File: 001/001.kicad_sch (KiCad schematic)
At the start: 16 parts, among them P1 Digital, P10 CONN_01X01, P11 CONN_01X01, P12 CONN_01X01, P13 CONN_01X01, P2 Power, P3 Analog, P4 Analog, P5 PWM, P6 PWM, P7 Communication, P8 CONN_01X01, P9 CONN_01X01

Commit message: 半分終了
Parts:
- added C?: 0.1uF, symbol akizuki:C
- added D? (x3): 1N4148, Diode_THT:D_DO-35_SOD27_P7.62mm_Horizontal, symbol Diode:1N4148
- added J?: GPS, symbol Connector_Generic:Conn_01x05
- added J?: iM920, symbol Connector_Generic:Conn_01x07
- added R? (x5): 10k, symbol Device:R_US
- added U?: 24LC256, symbol Memory_EEPROM:24LC256
- R?: value R_US -> 10k
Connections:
- net 19(Rx1) is gone; now on net 15(Rx3): P7.6 (Pin_6)
- net +3V3: now also J?.4 (Pin_4), R?.1, R?.1, R?.1
- net +5V: now also C?.2, J?.5 (Pin_5), R?.1, R?.1, U?.8 (VCC)
- net 14(Tx3): now also D?.1 (K)
- net 15(Rx3): now also J?.3 (Pin_3), J?.5 (Pin_5)
- net 18(Tx1): now also D?.1 (K)
- net 2(**): now also J?.2 (Pin_2)
- net 3(**): now also D?.1 (K)
- net 4(**): now also J?.1 (Pin_1)
- net 5(**): now also J?.7 (Pin_7)
- net GND: now also C?.1, J?.3 (Pin_3), J?.4 (Pin_4), U?.1 (A0), U?.2 (A1), U?.3 (A2), U?.4 (GND), U?.7 (WP)
- net SCL: now also R?.2, U?.6 (SCL)
- net SDA: now also R?.2, U?.5 (SDA)
- new net !RESET: D?.2 (A), J?.1 (Pin_1), R?.2
- new net RX: D?.2 (A), D?.2 (A), J?.2 (Pin_2), J?.6 (Pin_6), R?.2, R?.2
- no-connect marks 7 -> 12
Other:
- moved on the sheet: U?

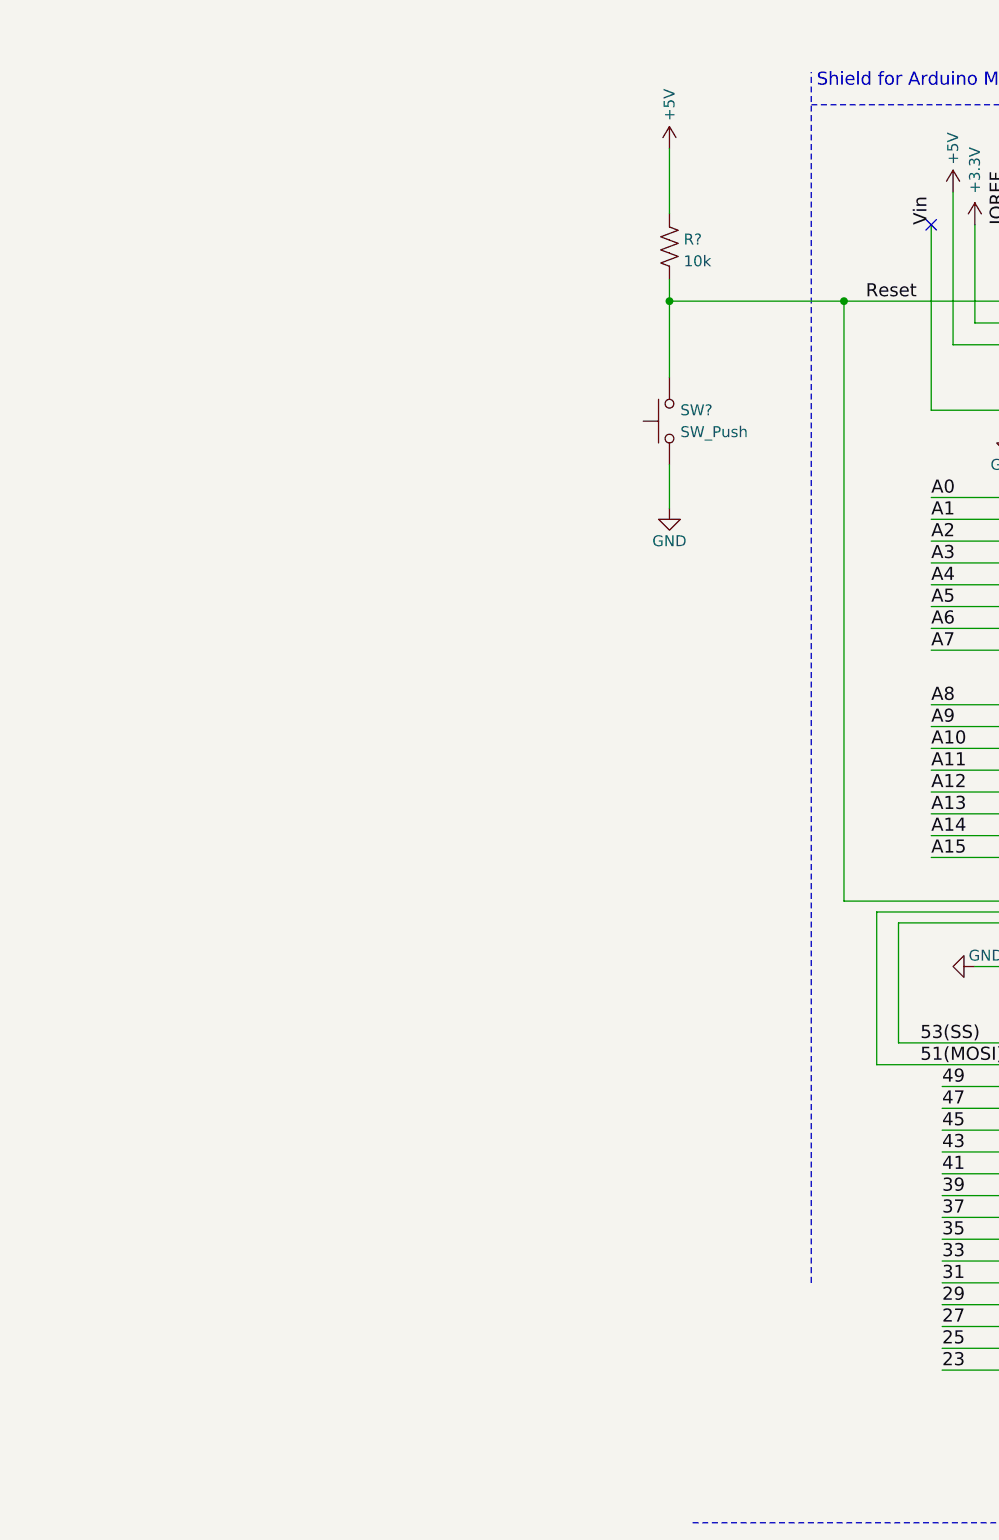
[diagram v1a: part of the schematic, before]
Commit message: RTC追加
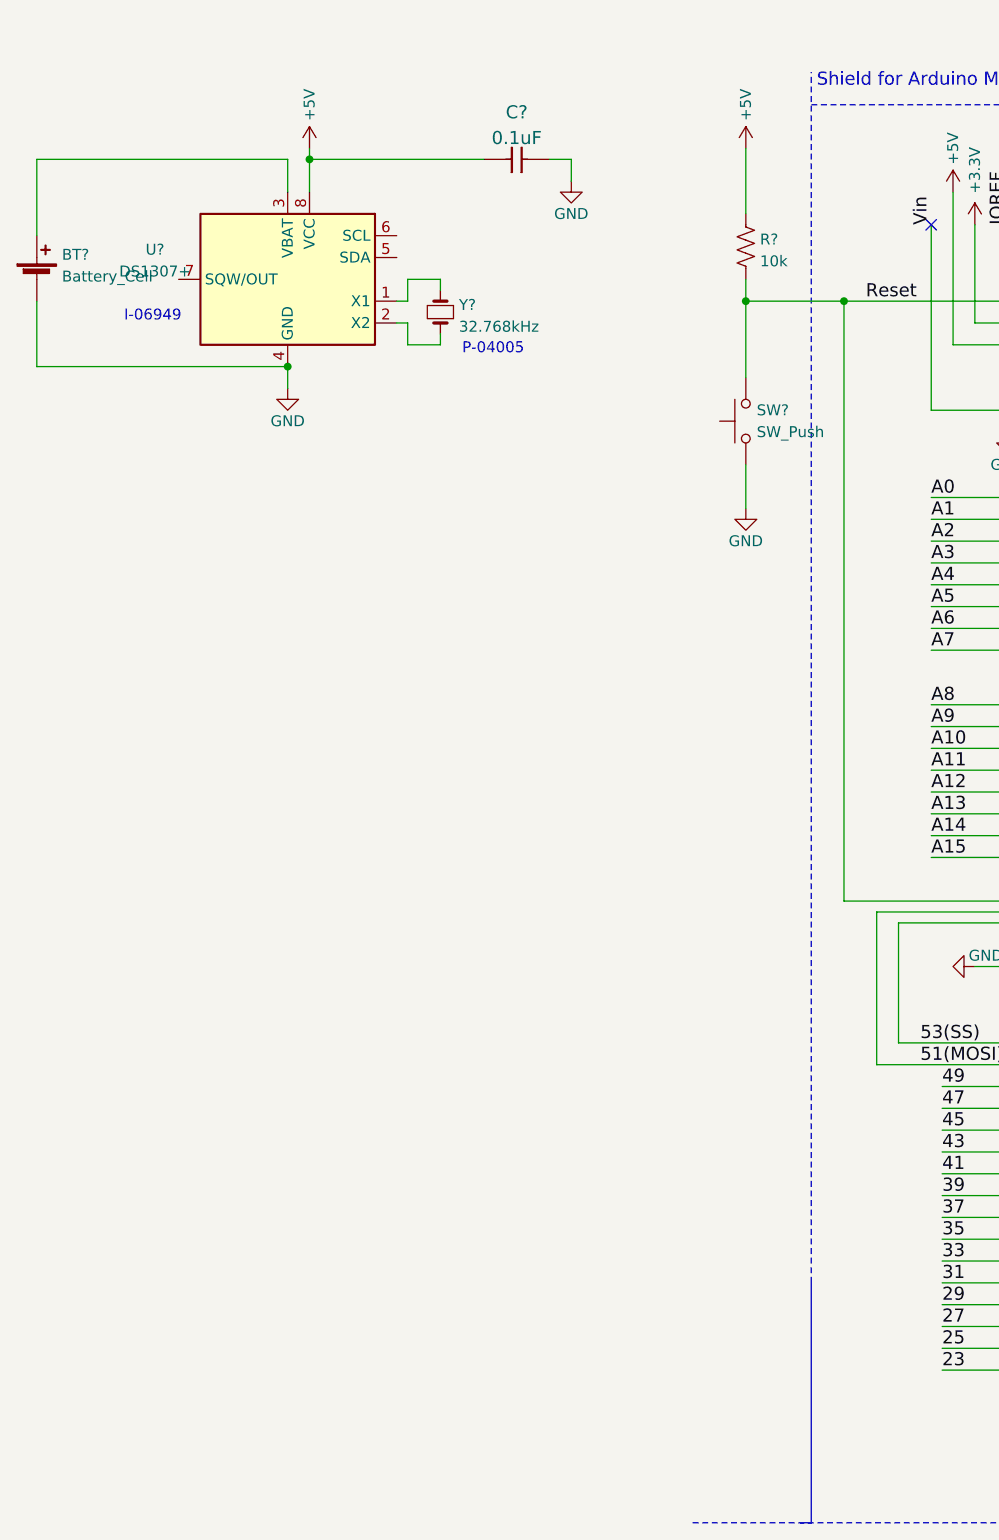
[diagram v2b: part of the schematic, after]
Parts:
- added BT?: Battery_Cell, symbol Device:Battery_Cell
- added C?: 0.1uF, symbol akizuki:C
- added U?: DS1307+, Package_DIP:DIP-8_W7.62mm, symbol Timer_RTC:DS1307+
- added Y?: 32.768kHz, symbol Device:Crystal_Small
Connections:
- net +5V: now also C?.2, U?.8 (VCC)
- net GND: now also BT?.2 (-), C?.1, U?.4 (GND)
- new net: U?.1 (X1), Y?.2
- new net: U?.2 (X2), Y?.1
- new net: BT?.1 (+), U?.3 (VBAT)
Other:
- note added: "I-06949"
- note added: "P-04005"
- moved on the sheet: R?, SW?

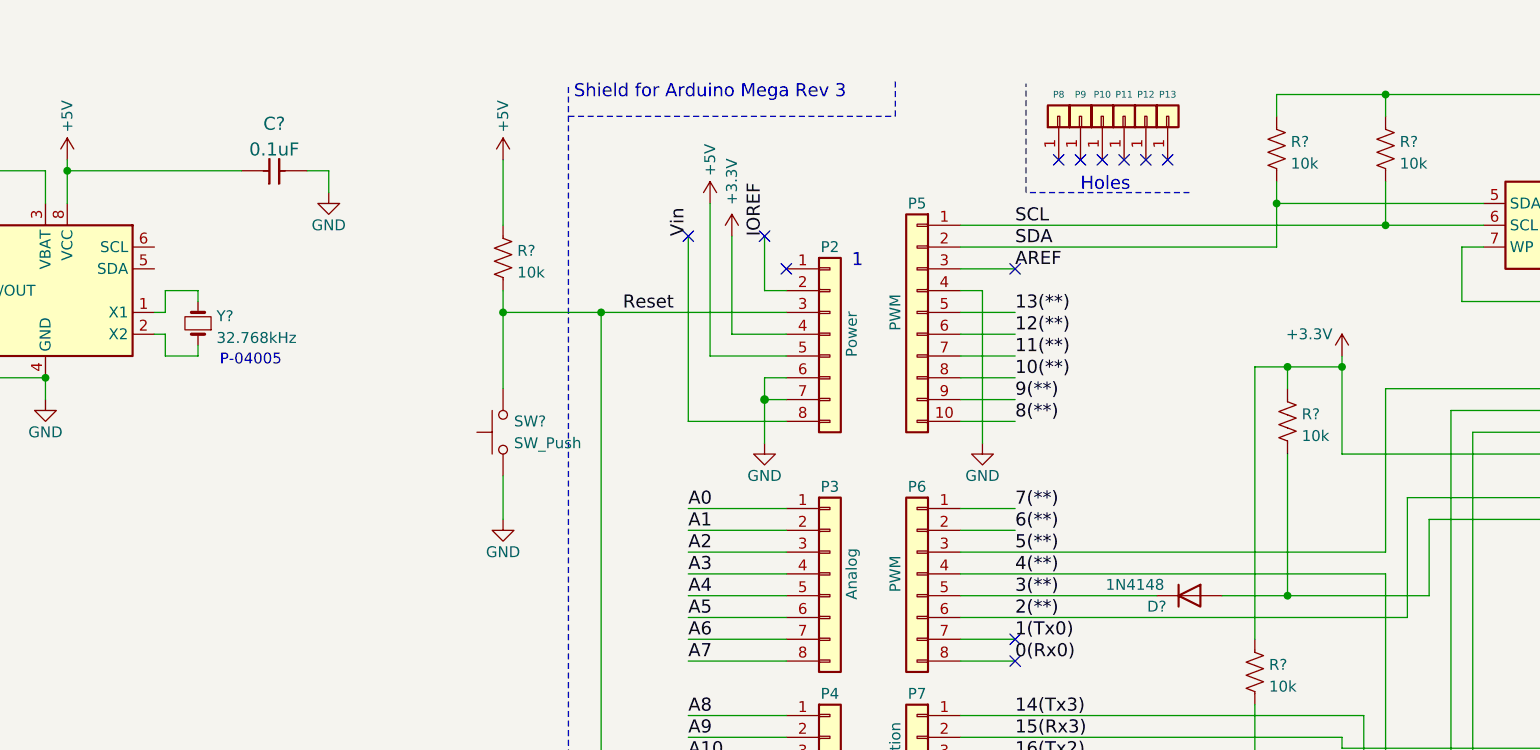
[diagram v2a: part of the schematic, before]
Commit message: Append RTC
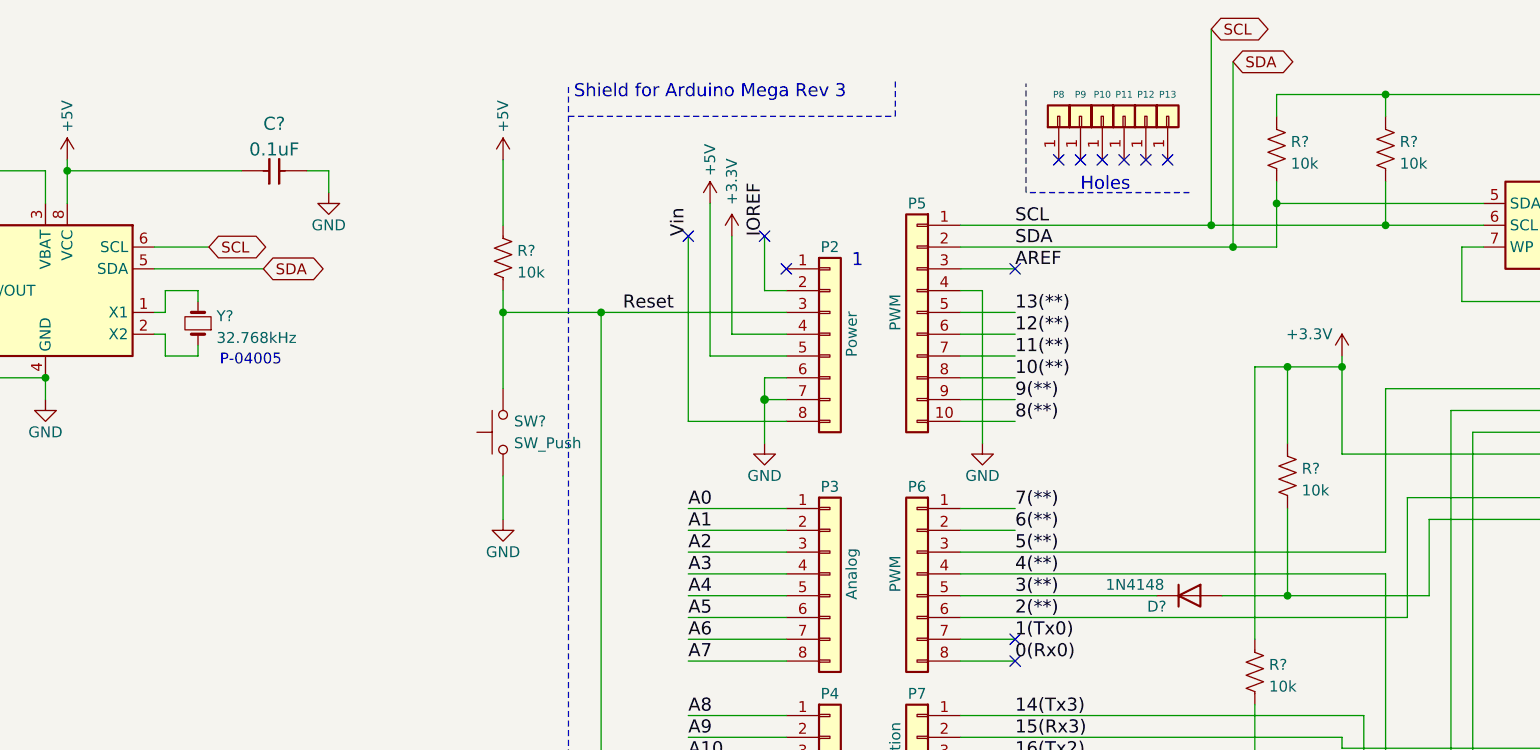
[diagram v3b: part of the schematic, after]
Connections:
- net SCL: now also U?.6 (SCL)
- net SDA: now also U?.5 (SDA)
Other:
- moved on the sheet: R?
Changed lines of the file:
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@@
   (junction (at 205.74 24.13) (diameter 0) (color 0 0 0 0)
+  )
+  (junction (at 187.96 41.91) (diameter 0) (color 0 0 0 0)
+  )
+  (junction (at 185.42 39.37) (diameter 0) (color 0 0 0 0)
   )
   (junction (at 102.87 49.53) (diameter 0) (color 0 0 0 0)
@@
     (stroke (width 0) (type default) (color 0 0 0 0))
   )
+  (wire (pts (xy 187.96 20.32) (xy 187.96 41.91))
+    (stroke (width 0) (type default) (color 0 0 0 0))
+  )
   (wire (pts (xy 241.3 143.51) (xy 246.38 143.51))
     (stroke (width 0) (type default) (color 0 0 0 0))
@@
     (stroke (width 0) (type default) (color 0 0 0 0))
   )
+  (wire (pts (xy 62.23 41.91) (xy 68.58 41.91))
+    (stroke (width 0) (type default) (color 0 0 0 0))
+  )
   (wire (pts (xy 118.11 138.43) (xy 133.35 138.43))
     (stroke (width 0) (type default) (color 0 0 0 0))
@@
     (stroke (width 0) (type solid) (color 0 0 0 0))
   )
-  (wire (pts (xy 156.21 39.37) (xy 205.74 39.37))
+  (wire (pts (xy 156.21 39.37) (xy 185.42 39.37))
     (stroke (width 0) (type solid) (color 0 0 0 0))
   )
@@
   )
   (wire (pts (xy 133.35 46.99) (xy 133.35 40.64))
+    (stroke (width 0) (type solid) (color 0 0 0 0))
+  )
+  (wire (pts (xy 187.96 41.91) (xy 193.04 41.91))
     (stroke (width 0) (type solid) (color 0 0 0 0))
   )
@@
     (stroke (width 0) (type solid) (color 0 0 0 0))
   )
-  (wire (pts (xy 156.21 41.91) (xy 193.04 41.91))
+  (wire (pts (xy 156.21 41.91) (xy 187.96 41.91))
     (stroke (width 0) (type solid) (color 0 0 0 0))
   )
@@
     (stroke (width 0) (type solid) (color 0 0 0 0))
   )
-  (wire (pts (xy 194.31 66.04) (xy 194.31 82.55))
+  (wire (pts (xy 194.31 72.39) (xy 194.31 82.55))
     (stroke (width 0) (type default) (color 0 0 0 0))
   )
@@
     (stroke (width 0) (type solid) (color 0 0 0 0))
   )
+  (wire (pts (xy 62.23 44.45) (xy 74.93 44.45))
+    (stroke (width 0) (type default) (color 0 0 0 0))
+  )
   (wire (pts (xy 114.3 49.53) (xy 135.89 49.53))
     (stroke (width 0) (type solid) (color 0 0 0 0))
@@
     (stroke (width 0) (type solid) (color 0 0 0 0))
   )
-  (wire (pts (xy 194.31 58.42) (xy 194.31 55.88))
+  (wire (pts (xy 194.31 64.77) (xy 194.31 55.88))
     (stroke (width 0) (type default) (color 0 0 0 0))
   )
@@
     (stroke (width 0) (type default) (color 0 0 0 0))
   )
+  (wire (pts (xy 185.42 39.37) (xy 205.74 39.37))
+    (stroke (width 0) (type solid) (color 0 0 0 0))
+  )
   (wire (pts (xy 114.3 49.53) (xy 114.3 119.38))
     (stroke (width 0) (type default) (color 0 0 0 0))
@@
   )
   (wire (pts (xy 200.66 100.33) (xy 200.66 99.06))
+    (stroke (width 0) (type default) (color 0 0 0 0))
+  )
+  (wire (pts (xy 185.42 16.51) (xy 185.42 39.37))
     (stroke (width 0) (type default) (color 0 0 0 0))
   )
@@
   (label "AREF" (at 162.56 44.45 0)
     (effects (font (size 1.524 1.524)) (justify left bottom))
+  )
+  (global_label "SDA" (shape bidirectional) (at 187.96 20.32 0) (fields_autoplaced)
+    (effects (font (size 1.27 1.27)) (justify left))
+    (property "シート間のリファレンス" "${INTERSHEET_REFS}" (id 0) (at 194.1317 20.2406 0)
+      (effects (font (size 1.27 1.27)) (justify left) hide)
+    )
+  )
+  (global_label "SCL" (shape bidirectional) (at 185.42 16.51 0) (fields_autoplaced)
+    (effects (font (size 1.27 1.27)) (justify left))
+    (property "シート間のリファレンス" "${INTERSHEET_REFS}" (id 0) (at 191.5312 16.4306 0)
+      (effects (font (size 1.27 1.27)) (justify left) hide)
+    )
+  )
+  (global_label "SCL" (shape bidirectional) (at 68.58 41.91 0) (fields_autoplaced)
+    (effects (font (size 1.27 1.27)) (justify left))
+    (property "シート間のリファレンス" "${INTERSHEET_REFS}" (id 0) (at 74.6912 41.8306 0)
+      (effects (font (size 1.27 1.27)) (justify left) hide)
+    )
+  )
+  (global_label "SDA" (shape bidirectional) (at 74.93 44.45 0) (fields_autoplaced)
+    (effects (font (size 1.27 1.27)) (justify left))
+    (property "シート間のリファレンス" "${INTERSHEET_REFS}" (id 0) (at 81.1017 44.3706 0)
+      (effects (font (size 1.27 1.27)) (justify left) hide)
+    )
   )
   (symbol (lib_id "Connector_Generic:Conn_01x01") (at 167.64 26.67 90) (unit 1)
@@
     (pin "2")
   )
-  (symbol (lib_id "Device:R_US") (at 194.31 62.23 0) (unit 1)
+  (symbol (lib_id "Device:R_US") (at 194.31 68.58 0) (unit 1)
     (in_bom yes) (on_board yes) (fields_autoplaced)
-    (property "Reference" "R?" (id 0) (at 195.961 61.3953 0)
+    (property "Reference" "R?" (id 0) (at 195.961 67.7453 0)
       (effects (font (size 1.27 1.27)) (justify left))
     )
-    (property "Value" "10k" (id 1) (at 195.961 63.9322 0)
+    (property "Value" "10k" (id 1) (at 195.961 70.2822 0)
       (effects (font (size 1.27 1.27)) (justify left))
     )
-    (property "Footprint" "" (id 2) (at 195.326 62.484 90)
-      (effects (font (size 1.27 1.27)) hide)
-    )
-    (property "Datasheet" "~" (id 3) (at 194.31 62.23 0)
-      (effects (font (size 1.27 1.27)) hide)
-    )
+    (property "Footprint" "" (id 2) (at 195.326 68.834 90)
+      (effects (font (size 1.27 1.27)) hide)
+    )
+    (property "Datasheet" "~" (id 3) (at 194.31 68.58 0)
+      (effects (font (size 1.27 1.27)) hide)
+    )
